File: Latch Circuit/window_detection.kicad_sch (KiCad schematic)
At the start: 0 parts

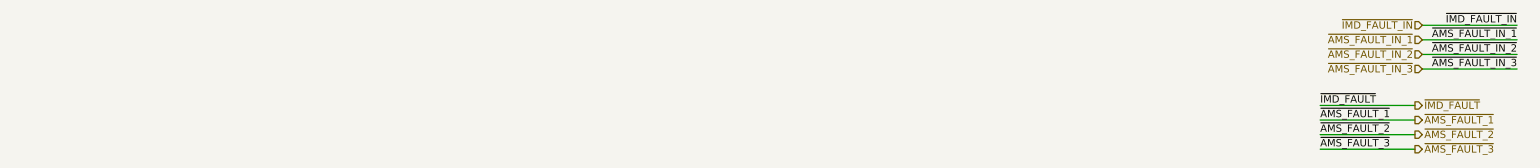
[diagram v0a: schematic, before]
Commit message: (wip) update OK condition inputs from IMD, AMS
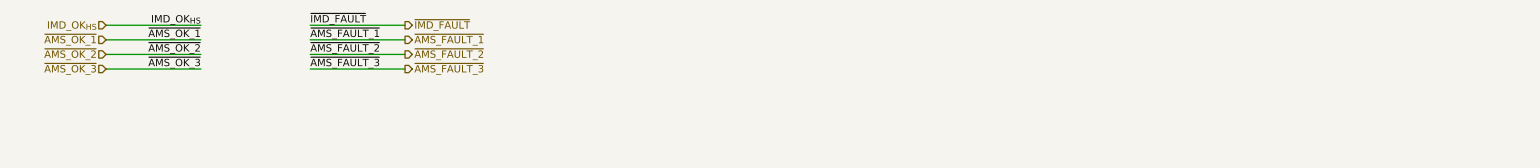
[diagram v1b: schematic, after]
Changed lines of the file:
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@@
 (kicad_sch (version 20211123) (generator eeschema)
   (paper "A4")
-  (wire (pts (xy 245.745 39.37) (xy 262.255 39.37))
+  (wire (pts (xy 69.85 25.4) (xy 86.36 25.4))
     (stroke (width 0) (type default) (color 0 0 0 0))
   )
-  (wire (pts (xy 263.525 20.32) (xy 280.035 20.32))
+  (wire (pts (xy 69.85 22.86) (xy 86.36 22.86))
     (stroke (width 0) (type default) (color 0 0 0 0))
   )
-  (wire (pts (xy 245.745 36.83) (xy 262.255 36.83))
+  (wire (pts (xy 69.85 17.78) (xy 86.36 17.78))
     (stroke (width 0) (type default) (color 0 0 0 0))
   )
-  (wire (pts (xy 245.745 31.75) (xy 262.255 31.75))
+  (wire (pts (xy 34.29 20.32) (xy 50.8 20.32))
     (stroke (width 0) (type default) (color 0 0 0 0))
   )
-  (wire (pts (xy 245.745 34.29) (xy 262.255 34.29))
+  (wire (pts (xy 34.29 25.4) (xy 50.8 25.4))
     (stroke (width 0) (type default) (color 0 0 0 0))
   )
-  (wire (pts (xy 263.525 22.86) (xy 280.035 22.86))
+  (wire (pts (xy 34.29 22.86) (xy 50.8 22.86))
     (stroke (width 0) (type default) (color 0 0 0 0))
   )
-  (wire (pts (xy 263.525 25.4) (xy 280.035 25.4))
+  (wire (pts (xy 69.85 20.32) (xy 86.36 20.32))
     (stroke (width 0) (type default) (color 0 0 0 0))
   )
-  (wire (pts (xy 263.525 17.78) (xy 280.035 17.78))
+  (wire (pts (xy 34.29 17.78) (xy 50.8 17.78))
     (stroke (width 0) (type default) (color 0 0 0 0))
   )
-  (label "~{IMD_FAULT_IN}" (at 280.035 17.78 180)
+  (label "~{AMS_OK_3}" (at 50.8 25.4 180)
     (effects (font (size 1.27 1.27)) (justify right bottom))
   )
-  (label "~{AMS_FAULT_IN_2}" (at 280.035 22.86 180)
+  (label "~{AMS_FAULT_1}" (at 69.85 20.32 0)
+    (effects (font (size 1.27 1.27)) (justify left bottom))
+  )
+  (label "~{AMS_OK_1}" (at 50.8 20.32 180)
     (effects (font (size 1.27 1.27)) (justify right bottom))
   )
-  (label "~{IMD_FAULT}" (at 245.745 31.75 0)
+  (label "~{AMS_FAULT_2}" (at 69.85 22.86 0)
     (effects (font (size 1.27 1.27)) (justify left bottom))
   )
-  (label "~{AMS_FAULT_IN_1}" (at 280.035 20.32 180)
+  (label "~{AMS_OK_2}" (at 50.8 22.86 180)
     (effects (font (size 1.27 1.27)) (justify right bottom))
   )
-  (label "~{AMS_FAULT_IN_3}" (at 280.035 25.4 180)
+  (label "IMD_OK_{HS}" (at 50.8 17.78 180)
     (effects (font (size 1.27 1.27)) (justify right bottom))
   )
-  (label "~{AMS_FAULT_1}" (at 245.745 34.29 0)
+  (label "~{IMD_FAULT}" (at 69.85 17.78 0)
     (effects (font (size 1.27 1.27)) (justify left bottom))
   )
-  (label "~{AMS_FAULT_2}" (at 245.745 36.83 0)
+  (label "~{AMS_FAULT_3}" (at 69.85 25.4 0)
     (effects (font (size 1.27 1.27)) (justify left bottom))
   )
-  (label "~{AMS_FAULT_3}" (at 245.745 39.37 0)
-    (effects (font (size 1.27 1.27)) (justify left bottom))
+  (hierarchical_label "IMD_OK_{HS}" (shape input) (at 34.29 17.78 180)
+    (effects (font (size 1.27 1.27)) (justify right))
   )
-  (hierarchical_label "~{AMS_FAULT_3}" (shape output) (at 262.255 39.37 0)
+  (hierarchical_label "~{AMS_FAULT_3}" (shape output) (at 86.36 25.4 0)
     (effects (font (size 1.27 1.27)) (justify left))
   )
-  (hierarchical_label "~{AMS_FAULT_IN_2}" (shape input) (at 263.525 22.86 180)
+  (hierarchical_label "~{AMS_OK_3}" (shape input) (at 34.29 25.4 180)
     (effects (font (size 1.27 1.27)) (justify right))
   )
-  (hierarchical_label "~{AMS_FAULT_1}" (shape output) (at 262.255 34.29 0)
+  (hierarchical_label "~{IMD_FAULT}" (shape output) (at 86.36 17.78 0)
     (effects (font (size 1.27 1.27)) (justify left))
   )
-  (hierarchical_label "~{AMS_FAULT_IN_3}" (shape input) (at 263.525 25.4 180)
+  (hierarchical_label "~{AMS_FAULT_1}" (shape output) (at 86.36 20.32 0)
+    (effects (font (size 1.27 1.27)) (justify left))
+  )
+  (hierarchical_label "~{AMS_OK_2}" (shape input) (at 34.29 22.86 180)
     (effects (font (size 1.27 1.27)) (justify right))
   )
-  (hierarchical_label "~{IMD_FAULT_IN}" (shape input) (at 263.525 17.78 180)
+  (hierarchical_label "~{AMS_OK_1}" (shape input) (at 34.29 20.32 180)
     (effects (font (size 1.27 1.27)) (justify right))
   )
-  (hierarchical_label "~{AMS_FAULT_2}" (shape output) (at 262.255 36.83 0)
+  (hierarchical_label "~{AMS_FAULT_2}" (shape output) (at 86.36 22.86 0)
     (effects (font (size 1.27 1.27)) (justify left))
   )
-  (hierarchical_label "~{AMS_FAULT_IN_1}" (shape input) (at 263.525 20.32 180)
-    (effects (font (size 1.27 1.27)) (justify right))
-  )
-  (hierarchical_label "~{IMD_FAULT}" (shape output) (at 262.255 31.75 0)
-    (effects (font (size 1.27 1.27)) (justify left))
-  )

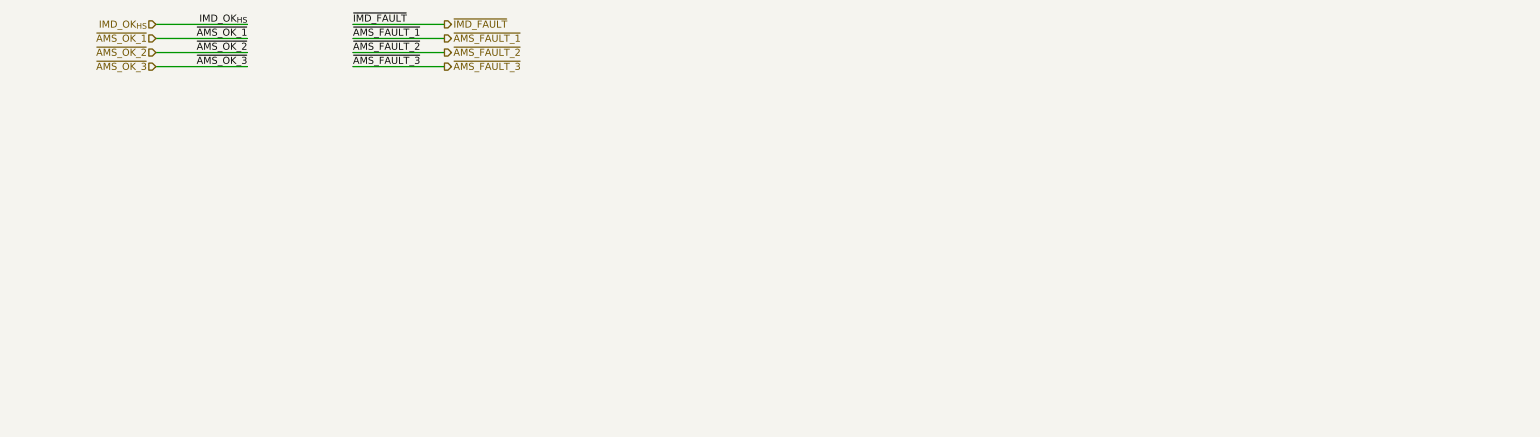
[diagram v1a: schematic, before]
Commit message: update schematic (ESF v1 submission)
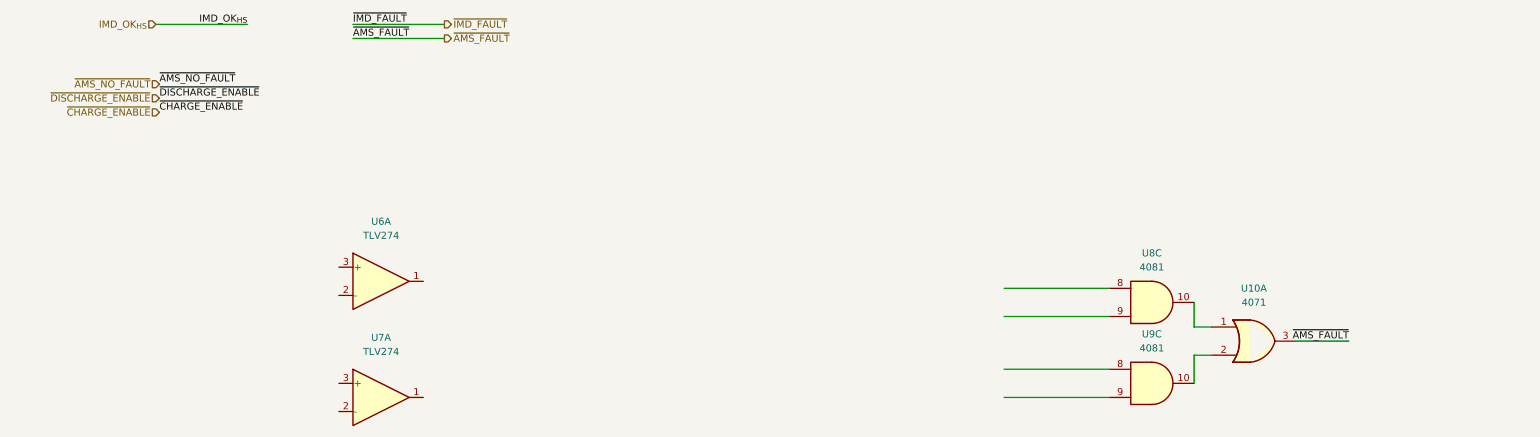
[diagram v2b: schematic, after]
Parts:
- added U10: 4071, Package_SO:SOIC-14_3.9x8.7mm_P1.27mm, symbol 4xxx:4071
- added U6, U7: TLV274, Package_SO:SOIC-14_3.9x8.7mm_P1.27mm, symbol Amplifier_Operational:TLC274
- added U8, U9: 4081, Package_SO:SOIC-14_3.9x8.7mm_P1.27mm, symbol 4xxx:4081
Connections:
- new net: U10.2, U9.10
- new net: U10.1, U8.10
- new net ~{AMS_FAULT}: U10.3
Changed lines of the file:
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@@
 (kicad_sch (version 20211123) (generator eeschema)
   (paper "A4")
-  (wire (pts (xy 69.85 25.4) (xy 86.36 25.4))
+  (wire (pts (xy 221.615 67.945) (xy 221.615 72.39))
     (stroke (width 0) (type default) (color 0 0 0 0))
   )
-  (wire (pts (xy 69.85 22.86) (xy 86.36 22.86))
+  (wire (pts (xy 224.79 77.47) (xy 221.615 77.47))
+    (stroke (width 0) (type default) (color 0 0 0 0))
+  )
+  (wire (pts (xy 187.325 65.405) (xy 206.375 65.405))
+    (stroke (width 0) (type default) (color 0 0 0 0))
+  )
+  (wire (pts (xy 221.615 72.39) (xy 224.79 72.39))
     (stroke (width 0) (type default) (color 0 0 0 0))
   )
@@
     (stroke (width 0) (type default) (color 0 0 0 0))
   )
-  (wire (pts (xy 34.29 20.32) (xy 50.8 20.32))
+  (wire (pts (xy 249.555 74.93) (xy 240.03 74.93))
     (stroke (width 0) (type default) (color 0 0 0 0))
   )
-  (wire (pts (xy 34.29 25.4) (xy 50.8 25.4))
+  (wire (pts (xy 187.325 80.01) (xy 206.375 80.01))
     (stroke (width 0) (type default) (color 0 0 0 0))
   )
-  (wire (pts (xy 34.29 22.86) (xy 50.8 22.86))
+  (wire (pts (xy 187.325 85.09) (xy 206.375 85.09))
+    (stroke (width 0) (type default) (color 0 0 0 0))
+  )
+  (wire (pts (xy 187.325 70.485) (xy 206.375 70.485))
+    (stroke (width 0) (type default) (color 0 0 0 0))
+  )
+  (wire (pts (xy 221.615 77.47) (xy 221.615 82.55))
     (stroke (width 0) (type default) (color 0 0 0 0))
   )
@@
     (stroke (width 0) (type default) (color 0 0 0 0))
   )
-  (label "~{AMS_OK_3}" (at 50.8 25.4 180)
-    (effects (font (size 1.27 1.27)) (justify right bottom))
-  )
-  (label "~{AMS_FAULT_1}" (at 69.85 20.32 0)
+  (label "~{AMS_FAULT}" (at 69.85 20.32 0)
     (effects (font (size 1.27 1.27)) (justify left bottom))
   )
-  (label "~{AMS_OK_1}" (at 50.8 20.32 180)
-    (effects (font (size 1.27 1.27)) (justify right bottom))
-  )
-  (label "~{AMS_FAULT_2}" (at 69.85 22.86 0)
+  (label "~{AMS_NO_FAULT}" (at 34.925 28.575 0)
     (effects (font (size 1.27 1.27)) (justify left bottom))
   )
-  (label "~{AMS_OK_2}" (at 50.8 22.86 180)
+  (label "~{DISCHARGE_ENABLE}" (at 34.925 31.115 0)
+    (effects (font (size 1.27 1.27)) (justify left bottom))
+  )
+  (label "~{AMS_FAULT}" (at 249.555 74.93 180)
     (effects (font (size 1.27 1.27)) (justify right bottom))
   )
@@
     (effects (font (size 1.27 1.27)) (justify left bottom))
   )
-  (label "~{AMS_FAULT_3}" (at 69.85 25.4 0)
+  (label "~{CHARGE_ENABLE}" (at 34.925 33.655 0)
     (effects (font (size 1.27 1.27)) (justify left bottom))
   )
@@
     (effects (font (size 1.27 1.27)) (justify right))
   )
-  (hierarchical_label "~{AMS_FAULT_3}" (shape output) (at 86.36 25.4 0)
-    (effects (font (size 1.27 1.27)) (justify left))
+  (hierarchical_label "~{CHARGE_ENABLE}" (shape input) (at 34.925 33.655 180)
+    (effects (font (size 1.27 1.27)) (justify right))
   )
-  (hierarchical_label "~{AMS_OK_3}" (shape input) (at 34.29 25.4 180)
+  (hierarchical_label "~{AMS_NO_FAULT}" (shape input) (at 34.925 28.575 180)
     (effects (font (size 1.27 1.27)) (justify right))
   )
@@
     (effects (font (size 1.27 1.27)) (justify left))
   )
-  (hierarchical_label "~{AMS_FAULT_1}" (shape output) (at 86.36 20.32 0)
+  (hierarchical_label "~{DISCHARGE_ENABLE}" (shape input) (at 34.925 31.115 180)
+    (effects (font (size 1.27 1.27)) (justify right))
+  )
+  (hierarchical_label "~{AMS_FAULT}" (shape output) (at 86.36 20.32 0)
     (effects (font (size 1.27 1.27)) (justify left))
   )
-  (hierarchical_label "~{AMS_OK_2}" (shape input) (at 34.29 22.86 180)
-    (effects (font (size 1.27 1.27)) (justify right))
+  (symbol (lib_id "Amplifier_Operational:TLC274") (at 74.93 64.135 0) (unit 1)
+    (in_bom yes) (on_board yes) (fields_autoplaced)
+    (property "Reference" "U6" (id 0) (at 74.93 53.34 0))
+    (property "Value" "TLV274" (id 1) (at 74.93 55.88 0))
+    (property "Footprint" "Package_SO:SOIC-14_3.9x8.7mm_P1.27mm" (id 2) (at 73.66 61.595 0)
+      (effects (font (size 1.27 1.27)) hide)
+    )
+    (property "Datasheet" "http://www.ti.com/lit/ds/symlink/tlc274.pdf" (id 3) (at 76.2 59.055 0)
+      (effects (font (size 1.27 1.27)) hide)
+    )
+    (pin "1")
+    (pin "2")
+    (pin "3")
   )
-  (hierarchical_label "~{AMS_OK_1}" (shape input) (at 34.29 20.32 180)
-    (effects (font (size 1.27 1.27)) (justify right))
+  (symbol (lib_id "4xxx:4081") (at 213.995 82.55 0) (unit 3)
+    (in_bom yes) (on_board yes) (fields_autoplaced)
+    (property "Reference" "U9" (id 0) (at 213.995 73.66 0))
+    (property "Value" "4081" (id 1) (at 213.995 76.2 0))
+    (property "Footprint" "Package_SO:SOIC-14_3.9x8.7mm_P1.27mm" (id 2) (at 213.995 82.55 0)
+      (effects (font (size 1.27 1.27)) hide)
+    )
+    (property "Datasheet" "http://www.intersil.com/content/dam/Intersil/documents/cd40/cd4073bms-81bms-82bms.pdf" (id 3) (at 213.995 82.55 0)
+      (effects (font (size 1.27 1.27)) hide)
+    )
+    (pin "10")
+    (pin "8")
+    (pin "9")
   )
-  (hierarchical_label "~{AMS_FAULT_2}" (shape output) (at 86.36 22.86 0)
-    (effects (font (size 1.27 1.27)) (justify left))
+  (symbol (lib_id "Amplifier_Operational:TLC274") (at 74.93 85.09 0) (unit 1)
+    (in_bom yes) (on_board yes) (fields_autoplaced)
+    (property "Reference" "U7" (id 0) (at 74.93 74.295 0))
+    (property "Value" "TLV274" (id 1) (at 74.93 76.835 0))
+    (property "Footprint" "Package_SO:SOIC-14_3.9x8.7mm_P1.27mm" (id 2) (at 73.66 82.55 0)
+      (effects (font (size 1.27 1.27)) hide)
+    )
+    (property "Datasheet" "http://www.ti.com/lit/ds/symlink/tlc274.pdf" (id 3) (at 76.2 80.01 0)
+      (effects (font (size 1.27 1.27)) hide)
+    )
+    (pin "1")
+    (pin "2")
+    (pin "3")
+  )
+  (symbol (lib_id "4xxx:4081") (at 213.995 67.945 0) (unit 3)
+    (in_bom yes) (on_board yes) (fields_autoplaced)
+    (property "Reference" "U8" (id 0) (at 213.995 59.055 0))
+    (property "Value" "4081" (id 1) (at 213.995 61.595 0))
+    (property "Footprint" "Package_SO:SOIC-14_3.9x8.7mm_P1.27mm" (id 2) (at 213.995 67.945 0)
+      (effects (font (size 1.27 1.27)) hide)
+    )
+    (property "Datasheet" "http://www.intersil.com/content/dam/Intersil/documents/cd40/cd4073bms-81bms-82bms.pdf" (id 3) (at 213.995 67.945 0)
+      (effects (font (size 1.27 1.27)) hide)
+    )
+    (pin "10")
+    (pin "8")
+    (pin "9")
+  )
+  (symbol (lib_id "4xxx:4071") (at 232.41 74.93 0) (unit 1)
+    (in_bom yes) (on_board yes) (fields_autoplaced)
+    (property "Reference" "U10" (id 0) (at 232.41 65.405 0))
+    (property "Value" "4071" (id 1) (at 232.41 67.945 0))
+    (property "Footprint" "Package_SO:SOIC-14_3.9x8.7mm_P1.27mm" (id 2) (at 232.41 74.93 0)
+      (effects (font (size 1.27 1.27)) hide)
+    )
+    (property "Datasheet" "http://www.intersil.com/content/dam/Intersil/documents/cd40/cd4071bms-72bms-75bms.pdf" (id 3) (at 232.41 74.93 0)
+      (effects (font (size 1.27 1.27)) hide)
+    )
+    (pin "1")
+    (pin "2")
+    (pin "3")
   )
 )
